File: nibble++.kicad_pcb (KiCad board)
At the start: 2 copper layers, 40 x 40 mm, 22 parts, among them SW1 SW_DPDT_x2, U1 NE555, U2 4017

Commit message: bump version number
Signed-off-by: Thomas Schmid <tom@binary-kitchen.de>
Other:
- board text added: "V1.1"
- board text removed: "V1.0"
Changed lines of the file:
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@@
     (effects (font (size 1.6 1.6) (thickness 0.1875)) (justify left mirror))
   )
-  (gr_text V1.0 (at 86.106 88.138) (layer B.SilkS)
+  (gr_text V1.1 (at 86.106 88.138) (layer B.SilkS)
     (effects (font (size 0.5 0.5) (thickness 0.11)) (justify mirror))
   )

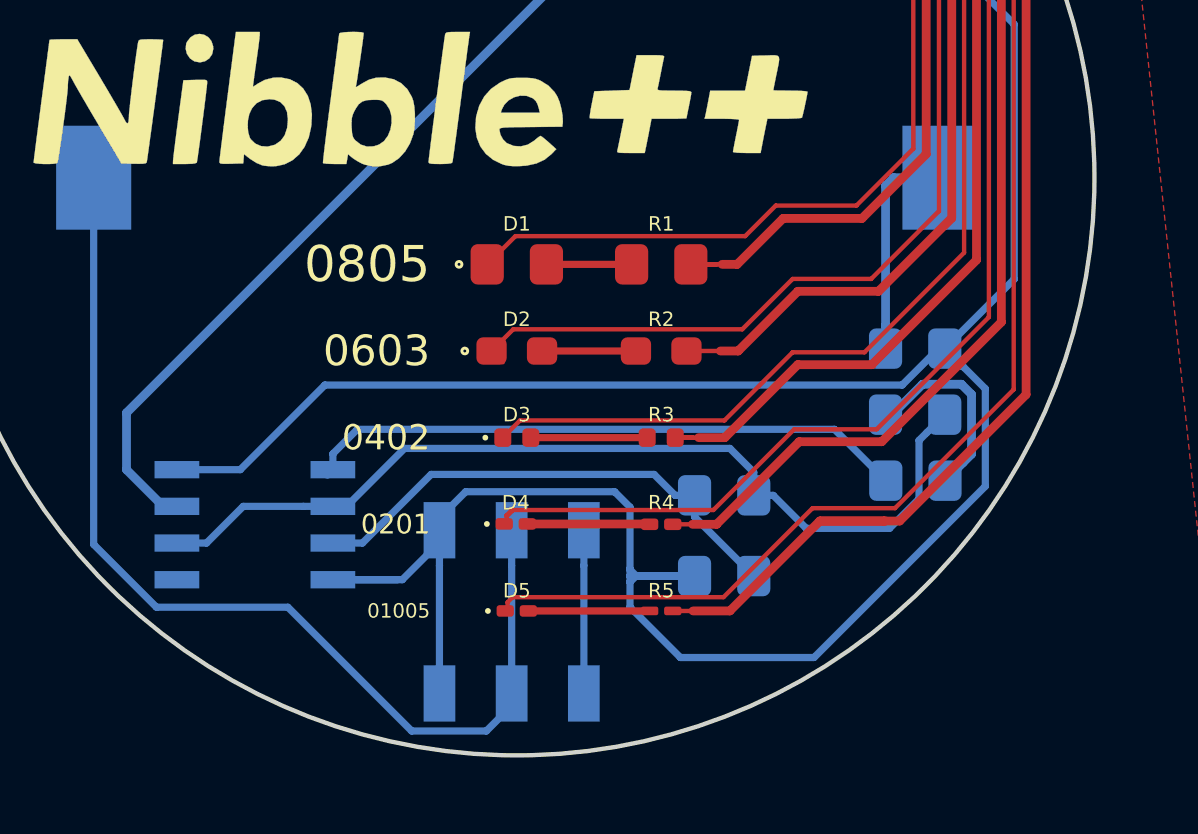
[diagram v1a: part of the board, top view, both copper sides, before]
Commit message: fixed #4
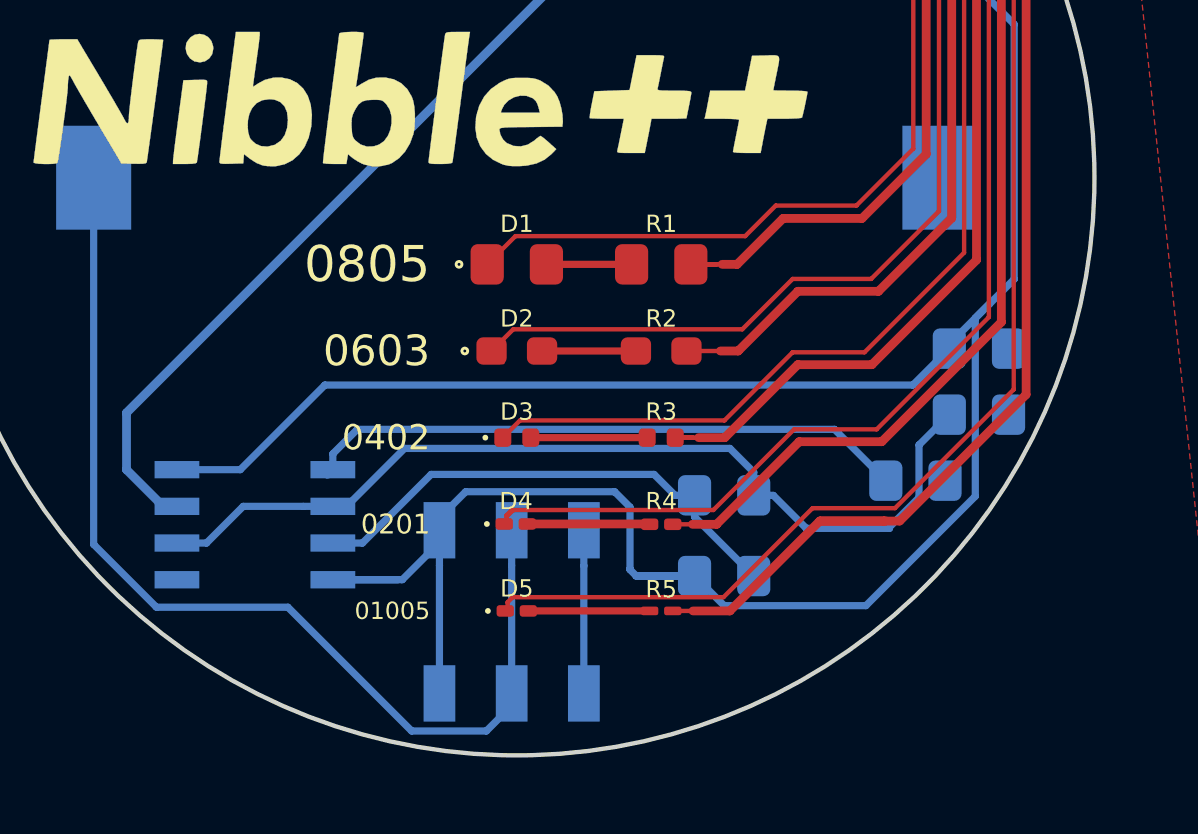
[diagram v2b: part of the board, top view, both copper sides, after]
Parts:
- moved C1 2.21 mm to (116.0, 105.9), turned to 180 degrees
- moved C2 2.21 mm to (116.0, 108.2), turned to 180 degrees
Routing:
- net GND: track 201.8 -> 187.3 mm
- net VS: track 108.9 -> 105.1 mm
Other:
- board text added: "V1.2"
- board text removed: "V1.1"
